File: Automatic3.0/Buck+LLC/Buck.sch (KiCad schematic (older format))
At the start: 26 parts, among them J1 OUT, J2 LED, J3 LED, J4 Conn_01x11, J5 LM324, J6 J, J7 Conn_01x01, J8 Conn_01x01, Q1 TIP122, Q2 TIP122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

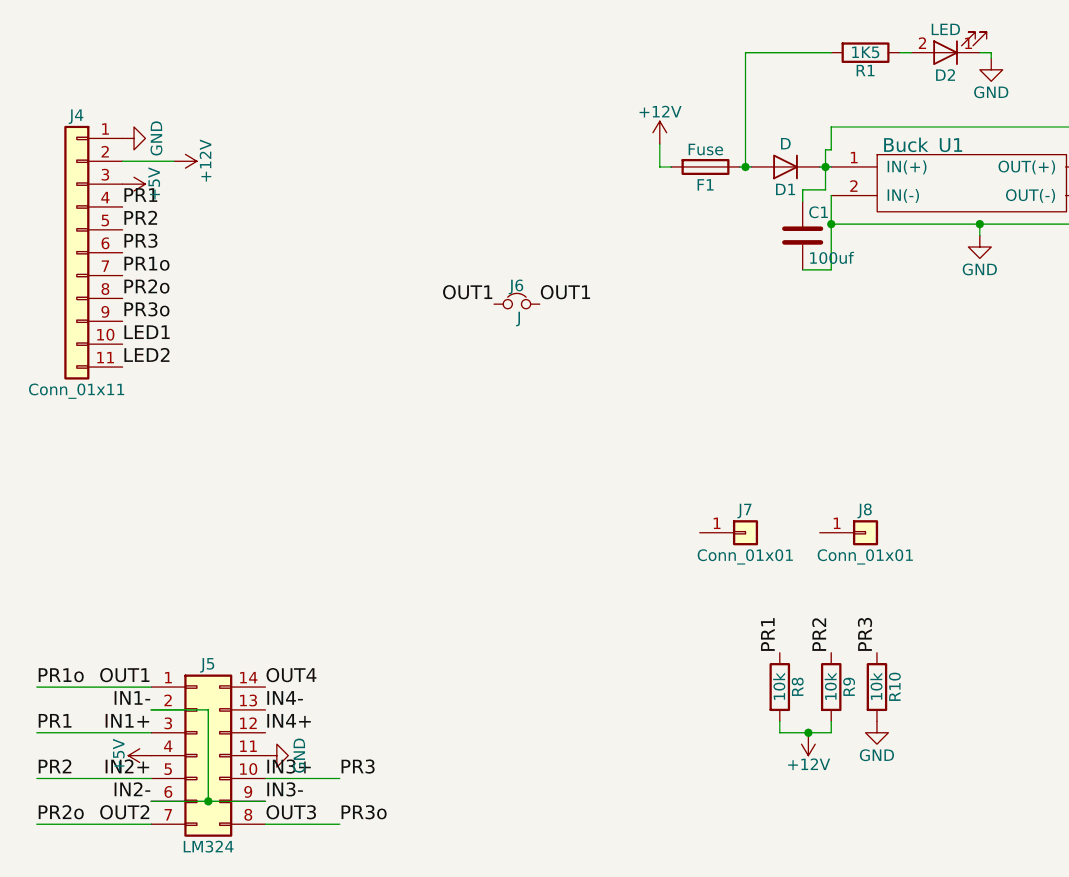
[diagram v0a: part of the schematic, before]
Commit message: Final automatic base circuits for ABU_ROBOCON_2018 completed
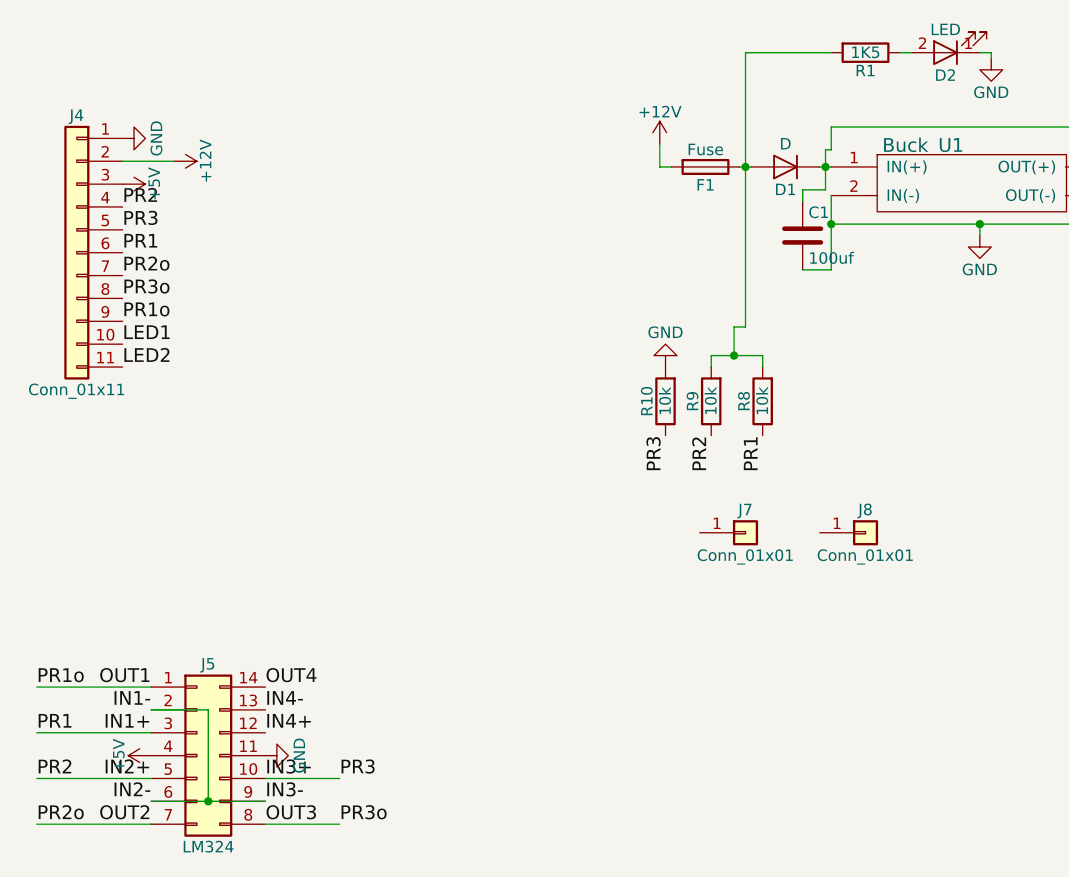
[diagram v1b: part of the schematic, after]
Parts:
- removed J6: J, modFiles:Jumper, symbol J
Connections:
- net +12V: no longer R8.2, R9.2
- net IN1+: now also J4.6 (Pin_6); no longer J4.4 (Pin_4)
- net IN2+: now also J4.4 (Pin_4); no longer J4.5 (Pin_5)
- net IN3+: now also J4.5 (Pin_5); no longer J4.6 (Pin_6)
- net OUT1: now also J4.9 (Pin_9); no longer J4.7 (Pin_7)
- net OUT2: now also J4.7 (Pin_7); no longer J4.8 (Pin_8)
- net OUT3: now also J4.8 (Pin_8); no longer J4.9 (Pin_9)
- net at D1.2 (A), F1.1, R1.2: now also R8.2, R9.2
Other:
- moved on the sheet: R10, R8, R9
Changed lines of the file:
@@
 	-1   0    0    -1
 $EndComp
+Text Label 1950 2525 0    60   ~ 0
+PR1
 Text Label 1950 2325 0    60   ~ 0
-PR1
+PR2
 Text Label 1950 2425 0    60   ~ 0
-PR2
-Text Label 1950 2525 0    60   ~ 0
 PR3
+Text Label 1950 2825 0    60   ~ 0
+PR1o
 Text Label 1950 2625 0    60   ~ 0
-PR1o
+PR2o
 Text Label 1950 2725 0    60   ~ 0
-PR2o
-Text Label 1950 2825 0    60   ~ 0
 PR3o
 Text Label 1950 2925 0    60   ~ 0
@@
 Text Label 1575 4825 0    60   ~ 0
 PR2
-Text Label 5250 4275 1    60   ~ 0
+Text Label 4325 3325 3    60   ~ 0
 PR3
 Text Label 1575 4425 0    60   ~ 0
@@
 	4925 2300 4925 2250
 Wire Wire Line
-	4925 2250 5025 2250
-Wire Wire Line
-	5025 2250 5025 2075
+	5025 2250 4925 2250
+Wire Wire Line
+	5025 2075 5025 2250
 Connection ~ 5025 2150
 Wire Wire Line
@@
 	5050 2075 5050 1975
 Wire Wire Line
-	4675 2150 4675 1650
+	4675 1650 4675 2850
 Wire Wire Line
 	4675 1650 5050 1650
@@
 Wire Wire Line
 	2900 5025 2575 5025
-$Comp
-L J J6
-U 1 1 5B4A5AFF
-P 3675 2750
-F 0 "J6" H 3675 2830 50  0000 C CNN
-F 1 "J" H 3685 2690 50  0000 C CNN
-F 2 "modFiles:Jumper" H 3675 2750 50  0001 C CNN
-F 3 "" H 3675 2750 50  0001 C CNN
-	1    3675 2750
-	1    0    0    -1
-$EndComp
-Text Label 3575 2750 2    60   ~ 0
-OUT1
-Text Label 3775 2750 0    60   ~ 0
-OUT1
 Wire Wire Line
 	9150 1975 9025 1975
@@
 L R R8
 U 1 1 5B5617D1
-P 4825 4425
-F 0 "R8" V 4905 4425 50  0000 C CNN
-F 1 "10k" V 4825 4425 50  0000 C CNN
-F 2 "modFiles:Resistor_small" V 4755 4425 50  0001 C CNN
-F 3 "" H 4825 4425 50  0001 C CNN
-	1    4825 4425
-	1    0    0    -1
+P 4750 3175
+F 0 "R8" V 4830 3175 50  0000 C CNN
+F 1 "10k" V 4750 3175 50  0000 C CNN
+F 2 "modFiles:Resistor_small" V 4680 3175 50  0001 C CNN
+F 3 "" H 4750 3175 50  0001 C CNN
+	1    4750 3175
+	-1   0    0    1
 $EndComp
 $Comp
 L R R9
 U 1 1 5B561992
-P 5050 4425
-F 0 "R9" V 5130 4425 50  0000 C CNN
-F 1 "10k" V 5050 4425 50  0000 C CNN
-F 2 "modFiles:Resistor_small" V 4980 4425 50  0001 C CNN
-F 3 "" H 5050 4425 50  0001 C CNN
-	1    5050 4425
-	1    0    0    -1
+P 4525 3175
+F 0 "R9" V 4605 3175 50  0000 C CNN
+F 1 "10k" V 4525 3175 50  0000 C CNN
+F 2 "modFiles:Resistor_small" V 4455 3175 50  0001 C CNN
+F 3 "" H 4525 3175 50  0001 C CNN
+	1    4525 3175
+	-1   0    0    1
 $EndComp
 $Comp
 L R R10
 U 1 1 5B5619FF
-P 5250 4425
-F 0 "R10" V 5330 4425 50  0000 C CNN
-F 1 "10k" V 5250 4425 50  0000 C CNN
-F 2 "modFiles:Resistor_small" V 5180 4425 50  0001 C CNN
-F 3 "" H 5250 4425 50  0001 C CNN
-	1    5250 4425
-	1    0    0    -1
-$EndComp
-$Comp
-L +12V #PWR012
-U 1 1 5B561AB3
-P 4950 4625
-F 0 "#PWR012" H 4950 4475 50  0001 C CNN
-F 1 "+12V" H 4950 4765 50  0000 C CNN
-F 2 "" H 4950 4625 50  0001 C CNN
-F 3 "" H 4950 4625 50  0001 C CNN
-	1    4950 4625
-	-1   0    0    1
-$EndComp
-Wire Wire Line
-	4825 4625 5050 4625
-Wire Wire Line
-	4825 4625 4825 4575
-Wire Wire Line
-	5050 4625 5050 4575
-Connection ~ 4950 4625
-$Comp
-L GND #PWR013
+P 4325 3175
+F 0 "R10" V 4405 3175 50  0000 C CNN
+F 1 "10k" V 4325 3175 50  0000 C CNN
+F 2 "modFiles:Resistor_small" V 4255 3175 50  0001 C CNN
+F 3 "" H 4325 3175 50  0001 C CNN
+	1    4325 3175
+	-1   0    0    1
+$EndComp
+Wire Wire Line
+	4525 2975 4750 2975
+Wire Wire Line
+	4750 2975 4750 3025
+Wire Wire Line
+	4525 2975 4525 3025
+Connection ~ 4625 2975
+$Comp
+L GND #PWR012
 U 1 1 5B561CAE
-P 5250 4575
-F 0 "#PWR013" H 5250 4325 50  0001 C CNN
-F 1 "GND" H 5250 4425 50  0000 C CNN
-F 2 "" H 5250 4575 50  0001 C CNN
-F 3 "" H 5250 4575 50  0001 C CNN
-	1    5250 4575
-	1    0    0    -1
-$EndComp
-Text Label 4825 4275 1    60   ~ 0
+P 4325 3025
+F 0 "#PWR012" H 4325 2775 50  0001 C CNN
+F 1 "GND" H 4325 2875 50  0000 C CNN
+F 2 "" H 4325 3025 50  0001 C CNN
+F 3 "" H 4325 3025 50  0001 C CNN
+	1    4325 3025
+	-1   0    0    1
+$EndComp
+Text Label 4750 3325 3    60   ~ 0
 PR1
-Text Label 5050 4275 1    60   ~ 0
+Text Label 4525 3325 3    60   ~ 0
 PR2
 Text Label 2900 4825 0    60   ~ 0
@@
 Wire Wire Line
 	9025 1900 8850 1900
+Wire Wire Line
+	4675 2850 4625 2850
+Wire Wire Line
+	4625 2850 4625 2975
 $EndSCHEMATC

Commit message: Final for ABU_ROBOCON_2018 Automatic_Base
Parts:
- removed J4: Conn_01x11, modFiles:BUCK+LLC, symbol Conn_01x11
- added J4: Conn_01x12, modFiles:BUCK+LLC, symbol Conn_01x12
- added J6: LED, modFiles:Connector_Bornier_2, symbol Conn_01x02
- added Q3: TIP122, modFiles:Voltage_Regulators, symbol TIP122
- added R11: 2K2, modFiles:Resistor_small, symbol R
- added R12: 10K, modFiles:Resistor_small, symbol R
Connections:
- net +12V: now also J4.2 (Pin_2)
- net +5V: now also J4.3 (Pin_3)
- net GND: now also J1.1 (Pin_1), J4.1 (Pin_1), Q3.3 (E), R12.2; no longer J1.2 (Pin_2)
- net IN1+: now also J4.6 (Pin_6)
- net IN2+: now also J4.4 (Pin_4)
- net IN3+: now also J4.5 (Pin_5)
- net LED1: now also J4.10 (Pin_10)
- net LED2: now also J4.11 (Pin_11)
- net OUT1: now also J4.9 (Pin_9)
- net OUT2: now also J4.7 (Pin_7)
- net OUT3: now also J4.8 (Pin_8)
- net at C1.1, D1.1 (K), R6.2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: no longer J2.1 (Pin_1), J3.1 (Pin_1)
- net at C2.1, U1.3 (OUT(+)): now also J1.2 (Pin_2); no longer J1.1 (Pin_1)
- net at D1.2 (A), F1.1, R1.2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: now also J2.1 (Pin_1), J3.1 (Pin_1), J6.1 (Pin_1)
- new net: Q3.1 (B), R11.1, R12.1
- new net: J6.2 (Pin_2), Q3.2 (C)
- new net LED3: J4.12 (Pin_12), R11.2
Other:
- moved on the sheet: R6, R7
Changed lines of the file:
@@
 L Conn_01x02 J1
 U 1 1 5B467096
-P 7000 2150
-F 0 "J1" H 7000 2250 50  0000 C CNN
-F 1 "OUT" H 7000 1950 50  0000 C CNN
-F 2 "modFiles:Connector_Bornier_2" H 7000 2150 50  0001 C CNN
-F 3 "" H 7000 2150 50  0001 C CNN
-	1    7000 2150
-	1    0    0    -1
+P 7000 2250
+F 0 "J1" H 7000 2350 50  0000 C CNN
+F 1 "OUT" H 7000 2050 50  0000 C CNN
+F 2 "modFiles:Connector_Bornier_2" H 7000 2250 50  0001 C CNN
+F 3 "" H 7000 2250 50  0001 C CNN
+	1    7000 2250
+	1    0    0    1
 $EndComp
 $Comp
@@
 Text Label 2575 4925 0    60   ~ 0
 IN3-
-Text Label 9450 1975 0    60   ~ 0
+Text Label 7175 875  0    60   ~ 0
 IN1-
 $Comp
 L GND #PWR08
 U 1 1 5B4917AD
-P 9150 2200
-F 0 "#PWR08" H 9150 1950 50  0001 C CNN
-F 1 "GND" H 9150 2050 50  0000 C CNN
-F 2 "" H 9150 2200 50  0001 C CNN
-F 3 "" H 9150 2200 50  0001 C CNN
-	1    9150 2200
+P 6875 1100
+F 0 "#PWR08" H 6875 850 50  0001 C CNN
+F 1 "GND" H 6875 950 50  0000 C CNN
+F 2 "" H 6875 1100 50  0001 C CNN
+F 3 "" H 6875 1100 50  0001 C CNN
+	1    6875 1100
 	1    0    0    -1
 $EndComp
@@
 L R R7
 U 1 1 5B4A2A6C
-P 9300 2125
-F 0 "R7" V 9380 2125 50  0000 C CNN
-F 1 "R" V 9300 2125 50  0000 C CNN
-F 2 "modFiles:Resistor_small" V 9230 2125 50  0001 C CNN
-F 3 "" H 9300 2125 50  0001 C CNN
-	1    9300 2125
+P 7025 1025
+F 0 "R7" V 7105 1025 50  0000 C CNN
+F 1 "R" V 7025 1025 50  0000 C CNN
+F 2 "modFiles:Resistor_small" V 6955 1025 50  0001 C CNN
+F 3 "" H 7025 1025 50  0001 C CNN
+	1    7025 1025
 	0    1    1    0
 $EndComp
@@
 L R R6
 U 1 1 5B4A2A13
-P 9300 1975
-F 0 "R6" V 9380 1975 50  0000 C CNN
-F 1 "R" V 9300 1975 50  0000 C CNN
-F 2 "modFiles:Resistor_small" V 9230 1975 50  0001 C CNN
-F 3 "" H 9300 1975 50  0001 C CNN
-	1    9300 1975
-	0    1    1    0
-$EndComp
-$Comp
-L Conn_01x11 J4
-U 1 1 5B4A3ADC
-P 1750 2525
-F 0 "J4" H 1750 3125 50  0000 C CNN
-F 1 "Conn_01x11" H 1750 1925 50  0000 C CNN
-F 2 "modFiles:BUCK+LLC" H 1750 2525 50  0001 C CNN
-F 3 "" H 1750 2525 50  0001 C CNN
-	1    1750 2525
-	-1   0    0    -1
+P 7025 875
+F 0 "R6" V 7105 875 50  0000 C CNN
+F 1 "R" V 7025 875 50  0000 C CNN
+F 2 "modFiles:Resistor_small" V 6955 875 50  0001 C CNN
+F 3 "" H 7025 875 50  0001 C CNN
+	1    7025 875
+	0    1    1    0
 $EndComp
 Text Label 1950 2525 0    60   ~ 0
@@
 	4925 2300 4925 2250
 Wire Wire Line
-	5025 2250 4925 2250
-Wire Wire Line
-	5025 2075 5025 2250
+	4925 2250 5025 2250
 Connection ~ 5025 2150
 Wire Wire Line
@@
 	6675 2250 6800 2250
 Connection ~ 6400 2500
-Wire Wire Line
-	5025 2075 5050 2075
 Wire Wire Line
 	5350 1650 5400 1650
@@
 	2175 2125 1950 2125
 Wire Wire Line
-	9450 1975 9450 2125
-Wire Wire Line
-	9150 2125 9150 2200
-Wire Wire Line
-	5050 2075 5050 1975
+	7175 875  7175 1025
+Wire Wire Line
+	6875 1025 6875 1100
 Wire Wire Line
 	4675 1650 4675 2850
@@
 Connection ~ 4675 2150
 Wire Wire Line
-	5050 1975 8850 1975
+	4675 1975 8850 1975
 Wire Wire Line
 	2075 4425 1575 4425
@@
 	2900 5025 2575 5025
 Wire Wire Line
-	9150 1975 9025 1975
+	6050 875  6875 875
 Wire Wire Line
 	9025 1975 9025 1900
@@
 Text Label 2900 4825 0    60   ~ 0
 PR3
-Connection ~ 9150 2175
+Connection ~ 6875 1075
 Connection ~ 9025 1900
 Connection ~ 8850 1975
 Wire Wire Line
-	9025 1900 8850 1900
+	8850 1900 10300 1900
 Wire Wire Line
 	4675 2850 4625 2850
 Wire Wire Line
 	4625 2850 4625 2975
+$Comp
+L TIP122 Q3
+U 1 1 5B5CFAED
+P 10150 3775
+F 0 "Q3" H 10400 3850 50  0000 L CNN
+F 1 "TIP122" H 10400 3775 50  0000 L CNN
+F 2 "modFiles:Voltage_Regulators" H 10400 3700 50  0001 L CIN
+F 3 "" H 10150 3775 50  0001 L CNN
+	1    10150 3775
+	1    0    0    -1
+$EndComp
+$Comp
+L R R11
+U 1 1 5B5CFAF3
+P 9750 3775
+F 0 "R11" V 9830 3775 50  0000 C CNN
+F 1 "2K2" V 9750 3775 50  0000 C CNN
+F 2 "modFiles:Resistor_small" V 9680 3775 50  0001 C CNN
+F 3 "" H 9750 3775 50  0001 C CNN
+	1    9750 3775
+	0    1    1    0
+$EndComp
+$Comp
+L R R12
+U 1 1 5B5CFAF9
+P 9925 4050
+F 0 "R12" V 10005 4050 50  0000 C CNN
+F 1 "10K" V 9925 4050 50  0000 C CNN
+F 2 "modFiles:Resistor_small" V 9855 4050 50  0001 C CNN
+F 3 "" H 9925 4050 50  0001 C CNN
+	1    9925 4050
+	1    0    0    -1
+$EndComp
+$Comp
+L GND #PWR013
+U 1 1 5B5CFAFF
+P 10250 4250
+F 0 "#PWR013" H 10250 4000 50  0001 C CNN
+F 1 "GND" H 10250 4100 50  0000 C CNN
+F 2 "" H 10250 4250 50  0001 C CNN
+F 3 "" H 10250 4250 50  0001 C CNN
+	1    10250 4250
+	1    0    0    -1
+$EndComp
+$Comp
+L Conn_01x02 J6
+U 1 1 5B5CFB05
+P 10500 3300
+F 0 "J6" H 10500 3400 50  0000 C CNN
+F 1 "LED" H 10500 3100 50  0000 C CNN
+F 2 "modFiles:Connector_Bornier_2" H 10500 3300 50  0001 C CNN
+F 3 "" H 10500 3300 50  0001 C CNN
+	1    10500 3300
+	1    0    0    -1
+$EndComp
+Text Label 9600 3775 2    60   ~ 0
+LED3
+Wire Wire Line
+	10300 1900 10300 3300
+Wire Wire Line
+	10300 3400 10250 3400
+Wire Wire Line
+	10250 3400 10250 3575
+Wire Wire Line
+	9900 3775 9950 3775
+Wire Wire Line
+	9925 3900 9925 3775
+Connection ~ 9925 3775
+Wire Wire Line
+	9925 4200 10250 4200
+Wire Wire Line
+	10250 3975 10250 4250
+Connection ~ 10250 4200
+$Comp
+L Conn_01x12 J4
+U 1 1 5B5D00A3
+P 1750 2525
+F 0 "J4" H 1750 3125 50  0000 C CNN
+F 1 "Conn_01x12" H 1750 1825 50  0000 C CNN
+F 2 "modFiles:BUCK+LLC" H 1750 2525 50  0001 C CNN
+F 3 "" H 1750 2525 50  0001 C CNN
+	1    1750 2525
+	-1   0    0    -1
+$EndComp
+Text Label 1950 3125 0    60   ~ 0
+LED3
+Wire Wire Line
+	5025 2250 5025 1950
+Connection ~ 4675 1975
+Wire Wire Line
+	6050 875  6050 1950
+Wire Wire Line
+	6050 1950 5025 1950
 $EndSCHEMATC
